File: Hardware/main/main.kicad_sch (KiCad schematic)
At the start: 1 part

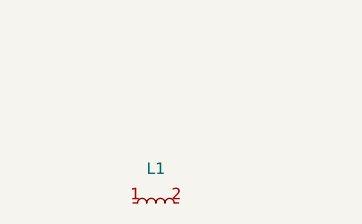
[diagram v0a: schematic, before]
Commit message: ETS  kicad güç şeması
ETS  kicad güç şeması çıkarıldı. Malzeme listesi belirlendi linkler eklenmedi.
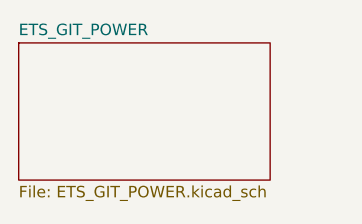
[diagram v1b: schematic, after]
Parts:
- removed L1: ~, symbol User_HB_Library_001:inductor_User_HB
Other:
- added sheet ETS_GIT_POWER (ETS_GIT_POWER.kicad_sch)
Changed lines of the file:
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@@
 		(date "2025-04-05")
 	)
-	(rule_area
-		(polyline
-			(pts
-				(xy 59.69 30.48) (xy 71.12 30.48) (xy 72.39 31.75) (xy 72.39 41.91) (xy 64.77 41.91) (xy 59.69 36.83)
-			)
-			(stroke
-				(width 0)
-				(type dash)
-			)
-			(fill
-				(type none)
-			)
-		)
-	)
-	(rule_area
-		(polyline
-			(pts
-				(xy 25.4 29.21) (xy 40.64 29.21) (xy 40.64 43.18) (xy 26.67 43.18) (xy 25.4 41.91)
-			)
-			(stroke
-				(width 0)
-				(type dash)
-			)
-			(fill
-				(type none)
-			)
-		)
-	)
-	(symbol
-		(lib_id "User_HB_Library_001:inductor_User_HB")
-		(at 31.75 39.37 0)
-		(unit 1)
+	(sheet
+		(at 16.51 20.32)
+		(size 27.94 15.24)
 		(exclude_from_sim no)
 		(in_bom yes)
@@
 		(dnp no)
 		(fields_autoplaced yes)
-		(property "Reference" "L1"
-			(at 31.75 34.29 0)
+		(stroke
+			(width 0.1524)
+			(type solid)
+		)
+		(fill
+			(color 0 0 0 0.0000)
+		)
+		(property "Sheetname" "ETS_GIT_POWER"
+			(at 16.51 19.6084 0)
 			(effects
 				(font
 					(size 1.27 1.27)
 				)
+				(justify left bottom)
 			)
 		)
-		(property "Value" "~"
-			(at 31.75 35.56 0)
+		(property "Sheetfile" "ETS_GIT_POWER.kicad_sch"
+			(at 16.51 36.1446 0)
 			(effects
 				(font
 					(size 1.27 1.27)
 				)
+				(justify left top)
 			)
 		)
-		(property "Footprint" ""
-			(at 31.75 39.37 0)
-			(effects
-				(font
-					(size 1.27 1.27)
-				)
-				(hide yes)
-			)
-		)
-		(property "Datasheet" ""
-			(at 31.75 39.37 0)
-			(effects
-				(font
-					(size 1.27 1.27)
-				)
-				(hide yes)
-			)
-		)
-		(property "Description" ""
-			(at 31.75 39.37 0)
-			(effects
-				(font
-					(size 1.27 1.27)
-				)
-				(hide yes)
-			)
-		)
-		(pin "1"
-		)
-		(pin "2"
-		)
 		(instances
-			(project ""
+			(project "main"
 				(path "/a940b775-bf67-4224-b5c3-1d071abb9d1b"
-					(reference "L1")
-					(unit 1)
+					(page "2")
 				)
 			)

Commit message: CANBUS Şematik Çizimi Bitti
CANBUS Şematik Çizimi Bitti
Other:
- added sheet ETS_GIT_CANBUS (ETS_GIT_CANBUS.kicad_sch)
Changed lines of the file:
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@@
+	)
+	(sheet
+		(at 52.07 20.32)
+		(size 22.86 15.24)
+		(exclude_from_sim no)
+		(in_bom yes)
+		(on_board yes)
+		(dnp no)
+		(fields_autoplaced yes)
+		(stroke
+			(width 0.1524)
+			(type solid)
+		)
+		(fill
+			(color 0 0 0 0.0000)
+		)
+		(property "Sheetname" "ETS_GIT_CANBUS"
+			(at 52.07 19.6084 0)
+			(effects
+				(font
+					(size 1.27 1.27)
+				)
+				(justify left bottom)
+			)
+		)
+		(property "Sheetfile" "ETS_GIT_CANBUS.kicad_sch"
+			(at 52.07 36.1446 0)
+			(effects
+				(font
+					(size 1.27 1.27)
+				)
+				(justify left top)
+			)
+		)
+		(instances
+			(project "main"
+				(path "/a940b775-bf67-4224-b5c3-1d071abb9d1b"
+					(page "3")
+				)
+			)
+		)
 	)
 	(sheet

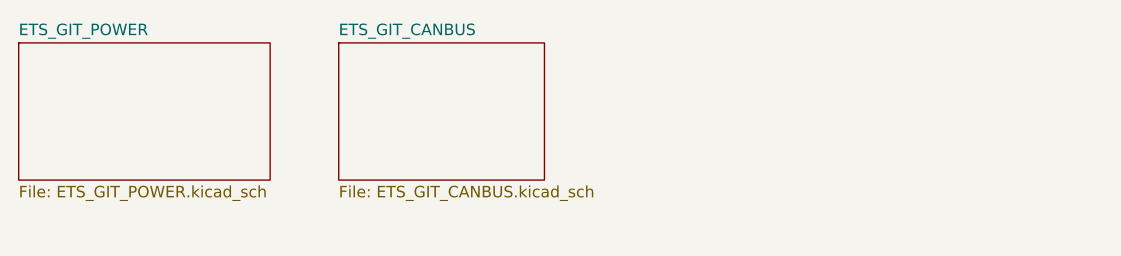
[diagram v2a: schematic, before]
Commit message: Ethernet devre çizimi v1
Ethernet devre çizimi temel atıldı eksikleri var
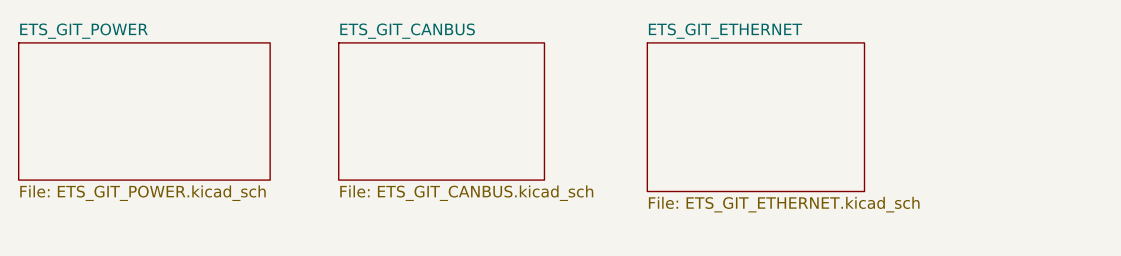
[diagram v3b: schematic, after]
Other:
- added sheet ETS_GIT_ETHERNET (ETS_GIT_ETHERNET.kicad_sch)
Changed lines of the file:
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@@
+	)
+	(sheet
+		(at 86.36 20.32)
+		(size 24.13 16.51)
+		(exclude_from_sim no)
+		(in_bom yes)
+		(on_board yes)
+		(dnp no)
+		(fields_autoplaced yes)
+		(stroke
+			(width 0.1524)
+			(type solid)
+		)
+		(fill
+			(color 0 0 0 0.0000)
+		)
+		(property "Sheetname" "ETS_GIT_ETHERNET"
+			(at 86.36 19.6084 0)
+			(effects
+				(font
+					(size 1.27 1.27)
+				)
+				(justify left bottom)
+			)
+		)
+		(property "Sheetfile" "ETS_GIT_ETHERNET.kicad_sch"
+			(at 86.36 37.4146 0)
+			(effects
+				(font
+					(size 1.27 1.27)
+				)
+				(justify left top)
+			)
+		)
+		(instances
+			(project "main"
+				(path "/a940b775-bf67-4224-b5c3-1d071abb9d1b"
+					(page "4")
+				)
+			)
+		)
 	)
 	(sheet

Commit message: ethernet schematik bitti
ethernet schematik bitti
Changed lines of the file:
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@@
 	)
 	(sheet
-		(at 52.07 20.32)
+		(at 63.5 22.86)
 		(size 22.86 15.24)
 		(exclude_from_sim no)
@@
 		)
 		(property "Sheetname" "ETS_GIT_CANBUS"
-			(at 52.07 19.6084 0)
+			(at 63.5 22.1484 0)
 			(effects
 				(font
@@
 		)
 		(property "Sheetfile" "ETS_GIT_CANBUS.kicad_sch"
-			(at 52.07 36.1446 0)
+			(at 63.5 38.6846 0)
 			(effects
 				(font
@@
 	)
 	(sheet
-		(at 86.36 20.32)
+		(at 97.79 22.86)
 		(size 24.13 16.51)
 		(exclude_from_sim no)
@@
 		)
 		(property "Sheetname" "ETS_GIT_ETHERNET"
-			(at 86.36 19.6084 0)
+			(at 97.79 22.1484 0)
 			(effects
 				(font
@@
 		)
 		(property "Sheetfile" "ETS_GIT_ETHERNET.kicad_sch"
-			(at 86.36 37.4146 0)
+			(at 97.79 39.9546 0)
 			(effects
 				(font
